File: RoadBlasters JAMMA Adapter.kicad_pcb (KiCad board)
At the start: 2 copper layers, 112.2 x 82 mm, 46 parts, among them J101 Molex_KK-396_5273-10A_1x10_P3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, J102 Molex_KK-254_AE-6410-02A_1x02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, J103 Molex_KK-254_AE-6410-02A_1x02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, J104 Molex_KK-254_AE-6410-02A_1x02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, J105 Molex_KK-254_AE-6410-04A_1x04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, J106 Molex_KK-254_AE-6410-02A_1x02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, J108 Molex_KK-254_AE-6410-05A_1x05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, P1 10K, U1 74LS86, U2 NE555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

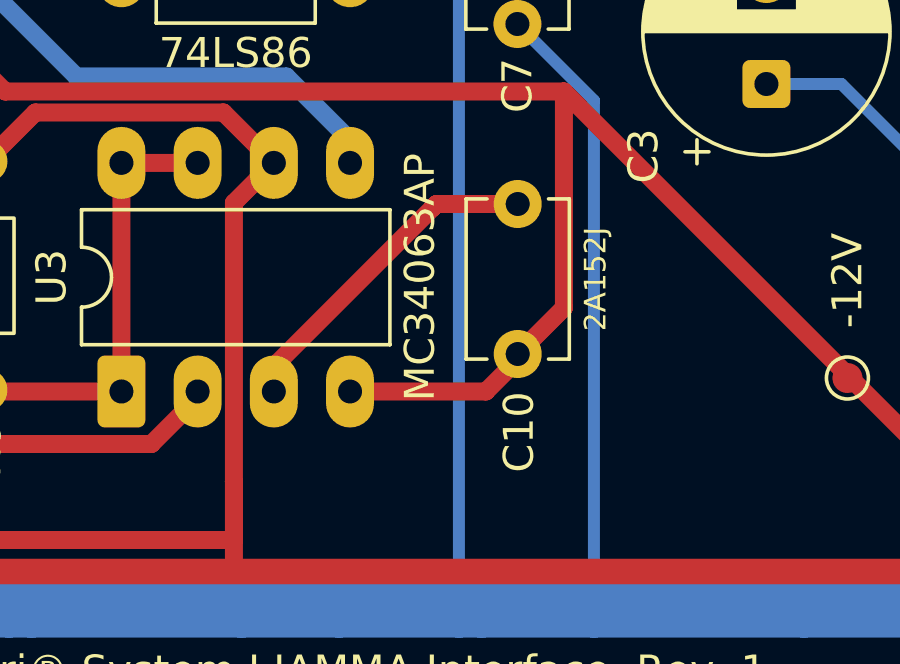
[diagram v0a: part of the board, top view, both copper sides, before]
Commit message: 3.4mm film caps for 152
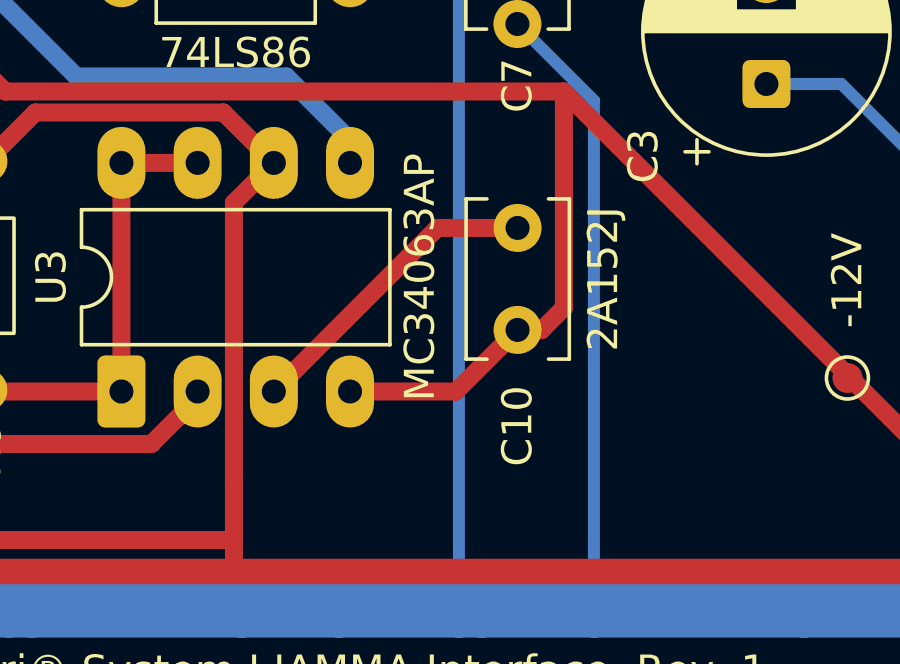
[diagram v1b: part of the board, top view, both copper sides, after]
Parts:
- C10: footprint Capacitor_THT:C_Disc_D5.1mm_W3.2mm_P5.00mm -> Capacitor_THT:C_Disc_D5.1mm_W3.2mm_P3.4mm
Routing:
- net U3_CAP: track 11.2 -> 10.4 mm
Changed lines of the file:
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@@
 		)
 	)
-	(footprint "Capacitor_THT:C_Disc_D5.1mm_W3.2mm_P5.00mm"
+	(footprint "Capacitor_THT:C_Disc_D5.1mm_W3.2mm_P3.4mm"
 		(layer "F.Cu")
 		(at 134.209874 110 90)
@@
 		(tags "C Disc series Radial pin pitch 5.00mm diameter 5.1mm width 3.2mm Capacitor")
 		(property "Reference" "C10"
-			(at -2.6 0.040126 90)
+			(at -2.4 -0.009874 90)
 			(layer "F.SilkS")
 			(effects
@@
 		)
 		(property "Value" "2A152J"
-			(at 2.5 2.590126 90)
+			(at 2.5 2.85 90)
 			(layer "F.SilkS")
 			(effects
 				(font
-					(size 0.72 0.72)
-					(thickness 0.108)
+					(size 1 1)
+					(thickness 0.15)
 				)
 			)
@@
 		)
 		(fp_rect
-			(start -1.05 -1.85)
-			(end 6.05 1.85)
+			(start -0.55 -1.85)
+			(end 5.55 1.85)
 			(stroke
 				(width 0.05)
@@
 			(effects
 				(font
-					(size 0.72 0.72)
+					(size 1 1)
 					(thickness 0.15)
 				)
@@
 		)
 		(pad "1" thru_hole circle
-			(at 0 0 90)
+			(at 0.80214 -0.005015 90)
 			(size 1.6 1.6)
 			(drill 0.8)
@@
 		)
 		(pad "2" thru_hole circle
-			(at 5 0 90)
+			(at 4.201914 -0.005015 90)
 			(size 1.6 1.6)
 			(drill 0.8)
@@
 	)
 	(segment
-		(start 133.15 111.25)
-		(end 128.62 111.25)
-		(width 0.6)
-		(layer "F.Cu")
-		(net 25)
-	)
-	(segment
 		(start 189.8 125.4)
 		(end 196.2 125.4)
@@
 	)
 	(segment
-		(start 134.209874 110)
-		(end 134.209874 110.190126)
-		(width 0.6)
-		(layer "F.Cu")
-		(net 25)
-	)
-	(segment
 		(start 114.5 99.875)
 		(end 114.625 99.875)
@@
 	)
 	(segment
-		(start 134.209874 110)
-		(end 135.75 108.459874)
-		(width 0.6)
-		(layer "F.Cu")
-		(net 25)
-	)
-	(segment
 		(start 174.4 116.4)
 		(end 176.95 113.85)
@@
 	)
 	(segment
+		(start 132.152719 111.25)
+		(end 134.204859 109.19786)
+		(width 0.6)
+		(layer "F.Cu")
+		(net 25)
+	)
+	(segment
 		(start 150.9 116.4)
 		(end 174.4 116.4)
@@
 	)
 	(segment
+		(start 128.62 111.25)
+		(end 132.152719 111.25)
+		(width 0.6)
+		(layer "F.Cu")
+		(net 25)
+	)
+	(segment
 		(start 135.75 101.25)
 		(end 117.125 101.25)
@@
 	)
 	(segment
+		(start 135.012014 109.19786)
+		(end 135.75 108.459874)
+		(width 0.6)
+		(layer "F.Cu")
+		(net 25)
+	)
+	(segment
+		(start 134.204859 109.19786)
+		(end 135.012014 109.19786)
+		(width 0.6)
+		(layer "F.Cu")
+		(net 25)
+	)
+	(segment
 		(start 116.25 91.62)
 		(end 117.12 90.75)
@@
 	)
 	(segment
-		(start 134.209874 110.190126)
-		(end 133.15 111.25)
-		(width 0.6)
-		(layer "F.Cu")
-		(net 25)
-	)
-	(segment
 		(start 113.25 103.38)
 		(end 113.25 102)
@@
 	)
 	(segment
-		(start 131.375 105.125)
-		(end 131.5 105)
-		(width 0.6)
-		(layer "F.Cu")
-		(net 31)
-	)
-	(segment
-		(start 126.08 110.42)
-		(end 126.08 111.25)
-		(width 0.6)
-		(layer "F.Cu")
-		(net 31)
-	)
-	(segment
-		(start 131.375 105.125)
-		(end 126.08 110.42)
+		(start 131.531914 105.798086)
+		(end 134.204859 105.798086)
 		(width 0.6)
 		(layer "F.Cu")
@@
 	)
 	(segment
-		(start 131.5 105)
-		(end 134.209874 105)
+		(start 126.08 111.25)
+		(end 131.531914 105.798086)
 		(width 0.6)
 		(layer "F.Cu")

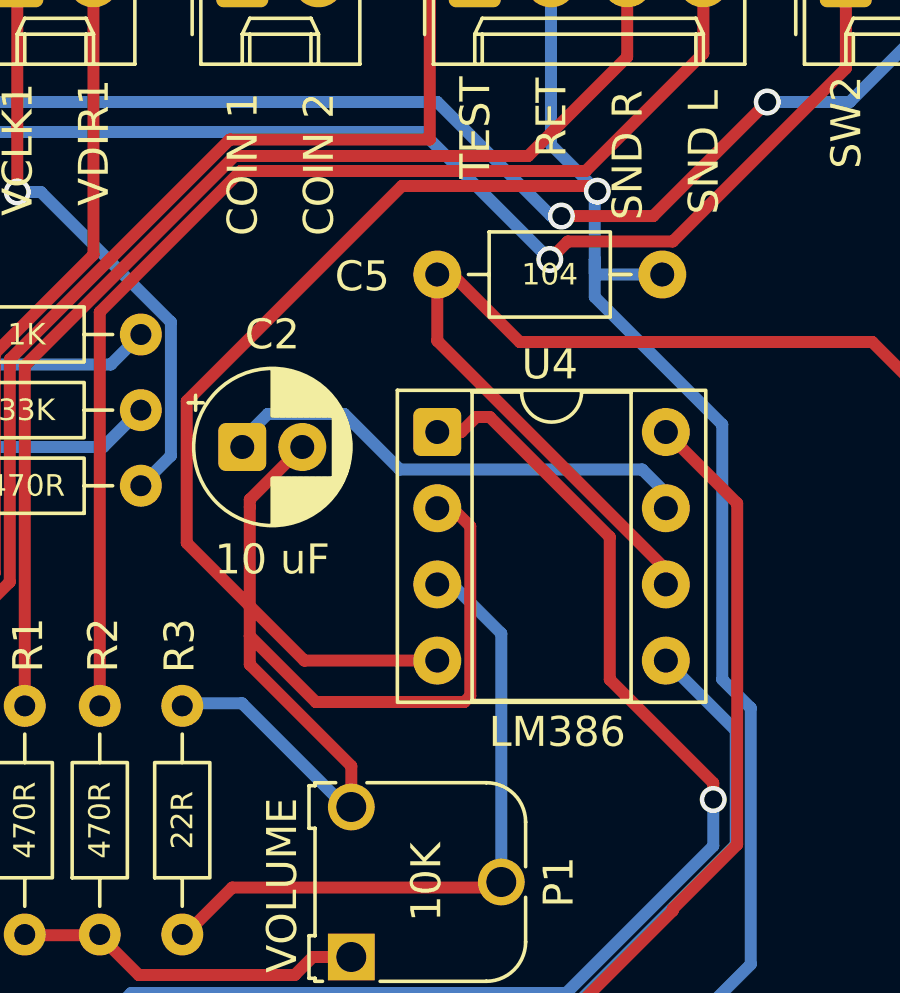
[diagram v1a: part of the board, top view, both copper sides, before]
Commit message: some rando on the internet didn't like how this was routed
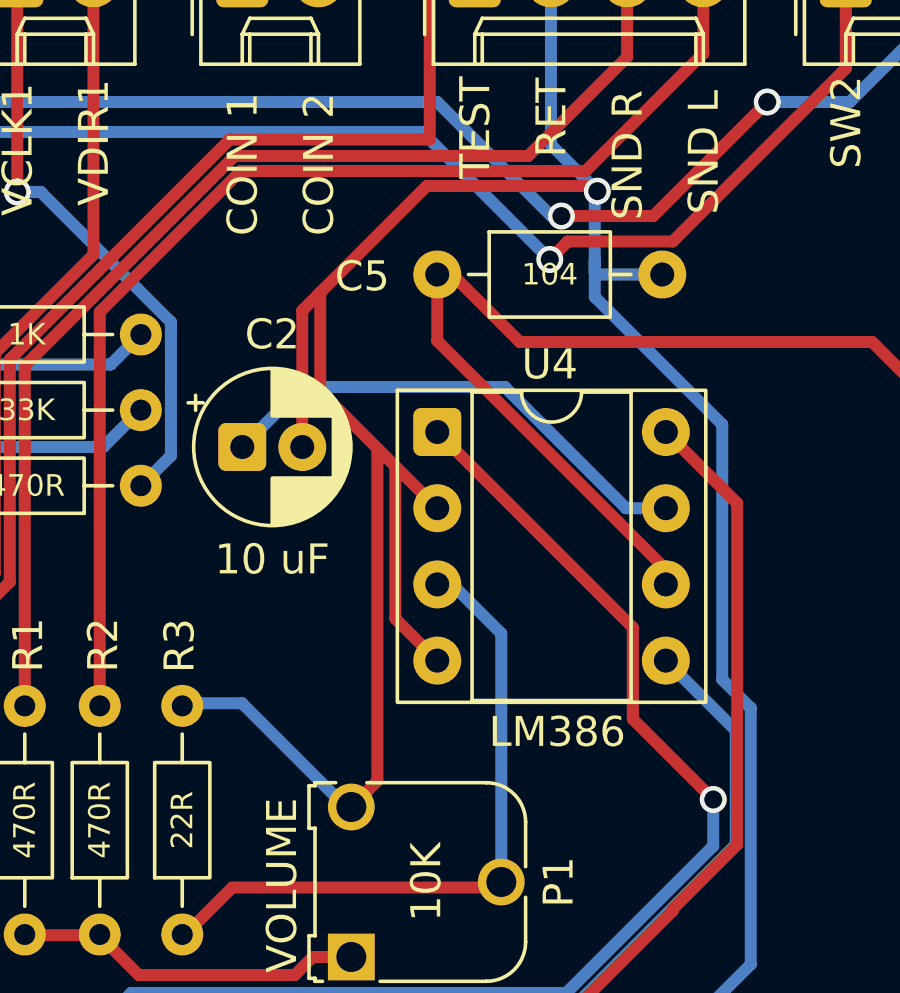
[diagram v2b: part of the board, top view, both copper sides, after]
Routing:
- net GND: track 758.5 -> 741.5 mm
- net U4_GAIN_P1: track 52.4 -> 50.7 mm
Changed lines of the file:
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@@
-	)
-	(segment
-		(start 156.399 89.199)
-		(end 156.399 84.472318)
-		(width 0.4)
-		(layer "F.Cu")
-		(net 1)
 	)
 	(segment
@@
 	)
 	(segment
-		(start 158.5 88)
-		(end 158.5 87.75)
-		(width 0.4)
-		(layer "F.Cu")
-		(net 1)
-	)
-	(segment
-		(start 161.885 96.635)
-		(end 158.5 93.25)
-		(width 0.4)
-		(layer "F.Cu")
-		(net 1)
-	)
-	(segment
 		(start 95.48 57.250066)
 		(end 95.48 50.930005)
 		(width 1.905)
-		(layer "F.Cu")
-		(net 1)
-	)
-	(segment
-		(start 164.75 88.04)
-		(end 165.25 88.04)
-		(width 0.4)
 		(layer "F.Cu")
 		(net 1)
@@
 	)
 	(segment
-		(start 161.885 98)
-		(end 161.885 96.635)
-		(width 0.4)
-		(layer "F.Cu")
-		(net 1)
-	)
-	(segment
-		(start 160.7 94.5)
-		(end 158.5 92.3)
-		(width 0.4)
-		(layer "F.Cu")
-		(net 1)
-	)
-	(segment
-		(start 165.652 94.5)
-		(end 160.7 94.5)
+		(start 162.755 86.045)
+		(end 160.85 84.14)
+		(width 0.4)
+		(layer "F.Cu")
+		(net 1)
+	)
+	(segment
+		(start 160.25 86)
+		(end 160.25 81.45)
+		(width 0.4)
+		(layer "F.Cu")
+		(net 1)
+	)
+	(segment
+		(start 163.355 86.645)
+		(end 162.755 86.045)
 		(width 0.4)
 		(layer "F.Cu")
@@
 	)
 	(segment
-		(start 164.25 93.12)
-		(end 164.75 93.12)
-		(width 0.4)
-		(layer "F.Cu")
-		(net 1)
-	)
-	(segment
-		(start 165.851 94.301)
-		(end 165.652 94.5)
+		(start 161.885 98)
+		(end 162.755 97.13)
+		(width 0.4)
+		(layer "F.Cu")
+		(net 1)
+	)
+	(segment
+		(start 163.355 86.645)
+		(end 163.355 91.725)
 		(width 0.4)
 		(layer "F.Cu")
@@
 	)
 	(segment
-		(start 158.5 91.3)
-		(end 156.399 89.199)
-		(width 0.4)
-		(layer "F.Cu")
-		(net 1)
-	)
-	(segment
-		(start 158.5 87.75)
-		(end 160.25 86)
+		(start 164.75 88.04)
+		(end 163.355 86.645)
+		(width 0.4)
+		(layer "F.Cu")
+		(net 1)
+	)
+	(segment
+		(start 163.355 91.725)
+		(end 164.75 93.12)
 		(width 0.4)
 		(layer "F.Cu")
@@
 	)
 	(segment
-		(start 169.91343 77.3)
-		(end 170.086069 77.472639)
-		(width 0.4)
-		(layer "F.Cu")
-		(net 1)
-	)
-	(segment
 		(start 95.529934 57.3)
 		(end 95.48 57.250066)
@@
 	)
 	(segment
+		(start 160.85 80.85)
+		(end 164.4 77.3)
+		(width 0.4)
+		(layer "F.Cu")
+		(net 1)
+	)
+	(segment
 		(start 191.985309 85.429182)
 		(end 191.985309 99.281473)
@@
 	)
 	(segment
-		(start 158.5 93.25)
-		(end 158.5 92.3)
-		(width 0.4)
-		(layer "F.Cu")
-		(net 1)
-	)
-	(segment
 		(start 144.642005 59.357995)
 		(end 144.642005 61.779571)
@@
 	)
 	(segment
+		(start 170.086069 77.472639)
+		(end 169.91343 77.3)
+		(width 0.4)
+		(layer "F.Cu")
+		(net 1)
+	)
+	(segment
+		(start 160.85 84.14)
+		(end 160.85 80.85)
+		(width 0.4)
+		(layer "F.Cu")
+		(net 1)
+	)
+	(segment
+		(start 162.755 97.13)
+		(end 162.755 86.045)
+		(width 0.4)
+		(layer "F.Cu")
+		(net 1)
+	)
+	(segment
 		(start 194.48 57.506356)
 		(end 194.48 57.3)
@@
 	)
 	(segment
-		(start 163.571318 77.3)
-		(end 169.91343 77.3)
-		(width 0.4)
-		(layer "F.Cu")
-		(net 1)
-	)
-	(segment
-		(start 156.399 84.472318)
-		(end 163.571318 77.3)
+		(start 160.25 81.45)
+		(end 160.85 80.85)
 		(width 0.4)
 		(layer "F.Cu")
@@
 		(start 100.75 61.5)
 		(end 96.500066 57.250066)
-		(width 0.4)
-		(layer "F.Cu")
-		(net 1)
-	)
-	(segment
-		(start 158.5 91.3)
-		(end 158.5 88)
-		(width 0.4)
-		(layer "F.Cu")
-		(net 1)
-	)
-	(segment
-		(start 165.25 88.04)
-		(end 165.851 88.641)
 		(width 0.4)
 		(layer "F.Cu")
@@
 	)
 	(segment
-		(start 165.851 88.641)
-		(end 165.851 94.301)
-		(width 0.4)
-		(layer "F.Cu")
-		(net 1)
-	)
-	(segment
 		(start 95.529934 57.527627)
 		(end 95.529934 57.3)
@@
 	)
 	(segment
-		(start 160.32 93.12)
-		(end 164.75 93.12)
-		(width 0.4)
-		(layer "F.Cu")
-		(net 1)
-	)
-	(segment
-		(start 158.5 92.3)
-		(end 158.5 91.3)
+		(start 169.91343 77.3)
+		(end 164.4 77.3)
 		(width 0.4)
 		(layer "F.Cu")
@@
 		(start 144.642005 61.779571)
 		(end 143.921576 62.5)
-		(width 0.4)
-		(layer "F.Cu")
-		(net 1)
-	)
-	(segment
-		(start 158.5 91.3)
-		(end 160.32 93.12)
 		(width 0.4)
 		(layer "F.Cu")
@@
 	)
 	(segment
-		(start 170.5 93.75)
-		(end 173.95 97.2)
+		(start 171.269 92.019)
+		(end 164.75 85.5)
 		(width 0.4)
 		(layer "F.Cu")
@@
 	)
 	(segment
-		(start 173.95 97.2)
-		(end 173.95 97.75)
+		(start 171.269 95.069)
+		(end 171.269 92.019)
 		(width 0.4)
 		(layer "F.Cu")
@@
 	)
 	(segment
-		(start 164.75 85.5)
-		(end 165.55 85.5)
-		(width 0.4)
-		(layer "F.Cu")
-		(net 21)
-	)
-	(segment
 		(start 157.4 112.6)
 		(end 152.994669 108.194669)
@@
 	)
 	(segment
-		(start 170.5 89)
-		(end 170.5 93.75)
-		(width 0.4)
-		(layer "F.Cu")
-		(net 21)
-	)
-	(segment
-		(start 165.55 85.5)
-		(end 166.05 85)
-		(width 0.4)
-		(layer "F.Cu")
-		(net 21)
-	)
-	(segment
-		(start 166.5 85)
-		(end 170.5 89)
-		(width 0.4)
-		(layer "F.Cu")
-		(net 21)
-	)
-	(segment
-		(start 166.05 85)
-		(end 166.5 85)
-		(width 0.4)
-		(layer "F.Cu")
-		(net 21)
-	)
-	(segment
 		(start 158.2 112.6)
 		(end 157.4 112.6)
+		(width 0.4)
+		(layer "F.Cu")
+		(net 21)
+	)
+	(segment
+		(start 173.95 97.75)
+		(end 171.269 95.069)
 		(width 0.4)
 		(layer "F.Cu")
@@
 	)
 	(segment
-		(start 159.101 84.899)
-		(end 158.25 85.75)
+		(start 171.04 88.04)
+		(end 167 84)
 		(width 0.4)
 		(layer "B.Cu")
@@
 	)
 	(segment
-		(start 163.5 86.75)
-		(end 161.649 84.899)
+		(start 167 84)
+		(end 160.25 84)
 		(width 0.4)
 		(layer "B.Cu")
@@
 	)
 	(segment
-		(start 158.25 85.75)
+		(start 160.25 84)
 		(end 158.25 86)
 		(width 0.4)
@@
 	)
 	(segment
-		(start 161.649 84.899)
-		(end 159.101 84.899)
-		(width 0.4)
-		(layer "B.Cu")
-		(net 23)
-	)
-	(segment
 		(start 172.37 88.04)
-		(end 172.37 87.54)
-		(width 0.4)
-		(layer "B.Cu")
-		(net 23)
-	)
-	(segment
-		(start 171.58 86.75)
-		(end 163.5 86.75)
-		(width 0.4)
-		(layer "B.Cu")
-		(net 23)
-	)
-	(segment
-		(start 172.37 87.54)
-		(end 171.58 86.75)
-		(width 0.4)
-		(layer "B.Cu")
+		(end 171.04 88.04)
+		(width 0.4)
+		(layer "B.Cu")
